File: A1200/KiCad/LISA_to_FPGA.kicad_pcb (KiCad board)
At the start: 2 copper layers, 64 x 37 mm, 18 parts, among them J1 Conn_01x04, J2 Conn_01x40, U1 LM1117-3.3, U2 74LVC16244ADGG, U3 74LVC16244ADGG, U4 LISA

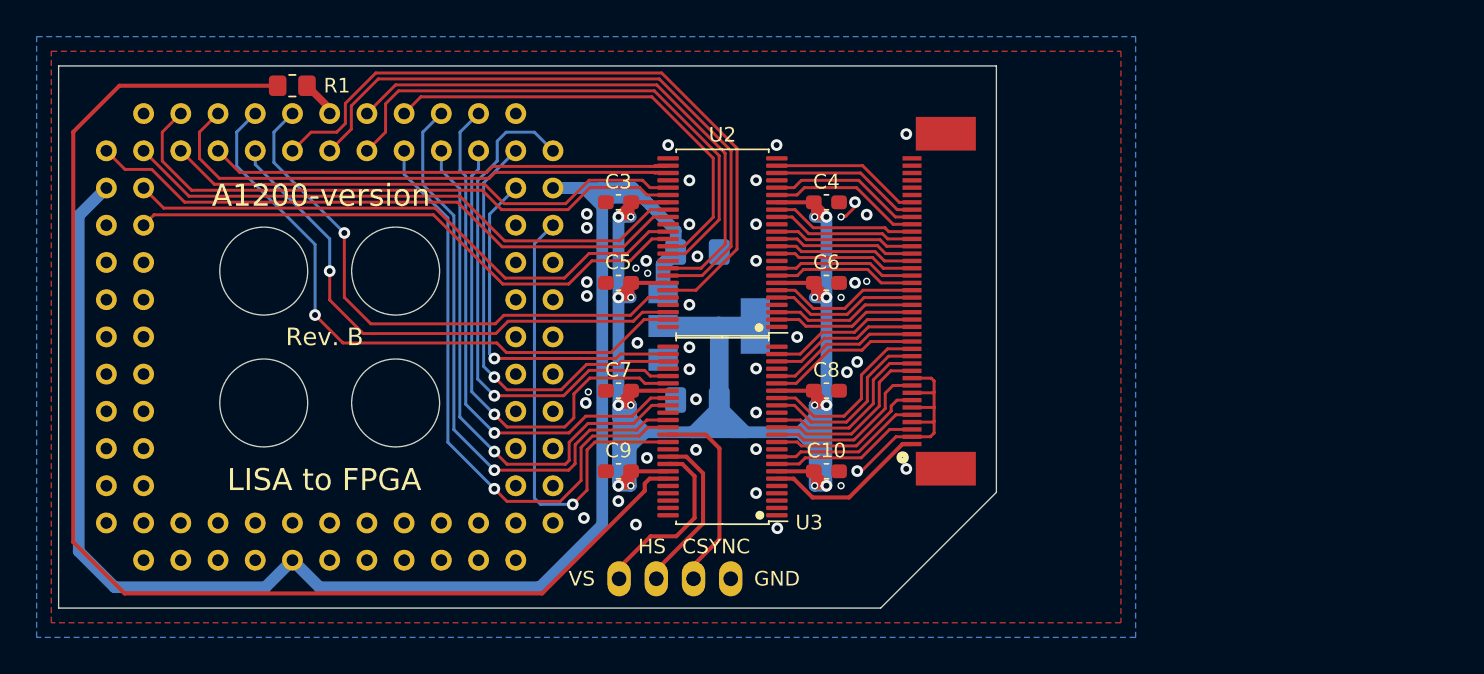
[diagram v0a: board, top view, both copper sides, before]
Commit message: Add a RP2354B to the design
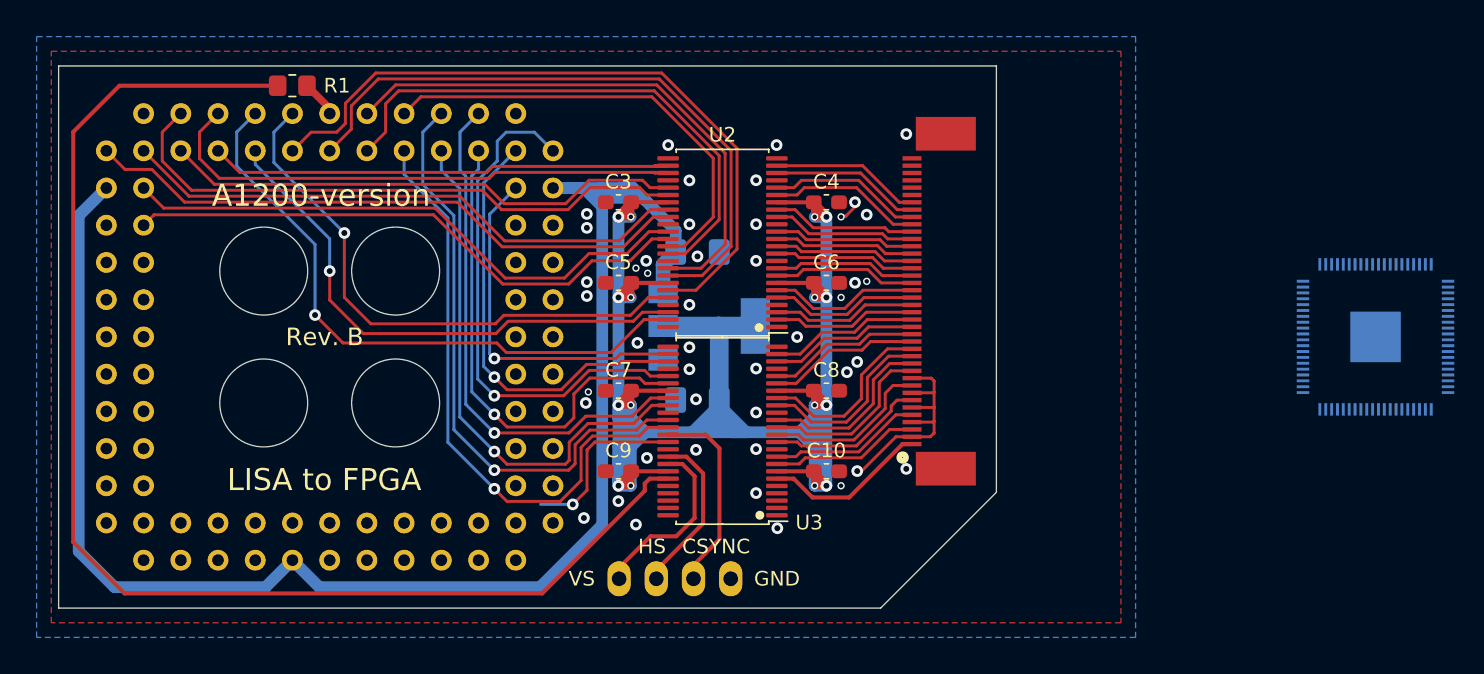
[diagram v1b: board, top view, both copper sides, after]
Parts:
- added U5: SC2212, LISA_to_FPGA:QFN40P1000X1000X90-81N-D, B.Cu at (238.1, 90.4)
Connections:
- net Net-(U4-Pad23) renamed C14O
- U4 pad 12: Net-(U4-Pad12) -> RGA8
- U4 pad 13: Net-(U4-Pad13) -> RGA7
- U4 pad 14: Net-(U4-Pad14) -> RGA6
- U4 pad 15: Net-(U4-Pad15) -> RGA5
- U4 pad 16: Net-(U4-Pad16) -> RGA4
- U4 pad 17: Net-(U4-Pad17) -> RGA3
- U4 pad 18: Net-(U4-Pad18) -> RGA2
- U4 pad 19: Net-(U4-Pad19) -> RGA1
- U4 pad 28: PIXELSW -> Net-(U4-Pad28)
- U4 pad 59: Net-(U4-Pad59) -> D31
- U4 pad 60: Net-(U4-Pad60) -> D30
- U4 pad 61: Net-(U4-Pad61) -> D29
- U4 pad 62: Net-(U4-Pad62) -> D28
- U4 pad 63: Net-(U4-Pad63) -> D27
- U4 pad 64: Net-(U4-Pad64) -> D26
- U4 pad 65: Net-(U4-Pad65) -> D25
- U4 pad 66: Net-(U4-Pad66) -> D24
- U4 pad 67: Net-(U4-Pad67) -> D23
- U4 pad 68: Net-(U4-Pad68) -> D22
- U4 pad 69: Net-(U4-Pad69) -> D21
- U4 pad 70: Net-(U4-Pad70) -> D20
- U4 pad 71: Net-(U4-Pad71) -> D19
- U4 pad 72: Net-(U4-Pad72) -> D18
- U4 pad 73: Net-(U4-Pad73) -> D17
- U4 pad 74: Net-(U4-Pad74) -> D16
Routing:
- net PIXELSW: track 31.8 -> 12.1 mm

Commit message: Change single resistors to 0603, add 330 OHm resistor packs, change U2,U3 to 74LVC162244ADGG with built-in 30 ohm termination resistors, fix to handsolder footprint for RP2354B, pin assignment and more routing
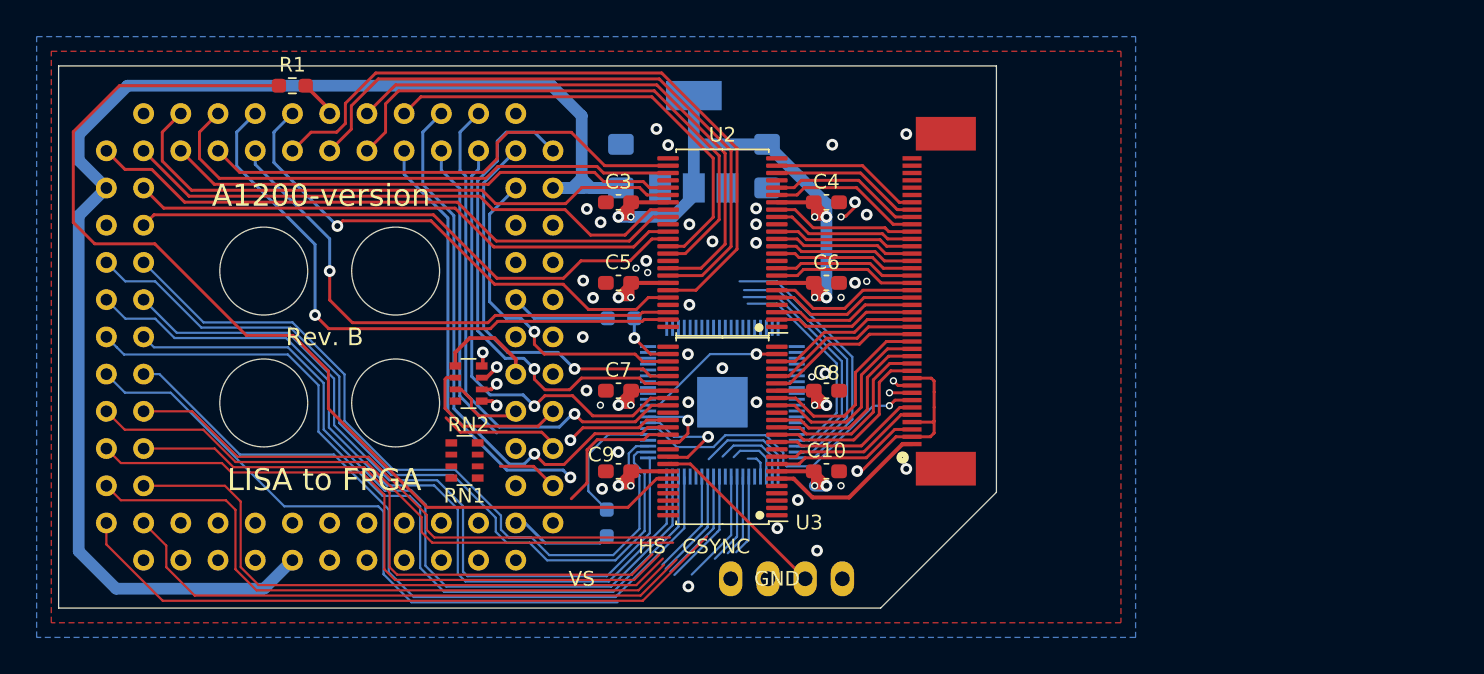
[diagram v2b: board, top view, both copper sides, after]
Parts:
- added R2: 330, Resistor_SMD:R_0603_1608Metric_Pad0.98x0.95mm_HandSolder, B.Cu at (185.7, 103.1)
- added R3: 100, Resistor_SMD:R_0603_1608Metric_Pad0.98x0.95mm_HandSolder, B.Cu at (186.6, 89.2)
- added RN1: R_Pack04, Resistor_SMD:R_Array_Convex_4x0603, F.Cu at (176.0, 98.9)
- added RN2: R_Pack04, Resistor_SMD:R_Array_Convex_4x0603, F.Cu at (176.2, 93.6)
- R1: value 33Ω -> 68; footprint Resistor_SMD:R_0805_2012Metric_Pad1.20x1.40mm_HandSolder -> Resistor_SMD:R_0603_1608Metric_Pad0.98x0.95mm_HandSolder
- U2, U3: value 74LVC16244ADGG -> 74LVC162244ADGG
- moved U5 44.8 mm to (193.6, 94.9), turned to 90 degrees
- moved C2 16.7 mm to (196.6, 78.8), turned to 90 degrees
- moved U1 12.6 mm to (191.6, 77.1), turned to 90 degrees
- moved C1 7.85 mm to (186.6, 78.8), turned to 270 degrees
- moved J1 7.62 mm to (201.8, 106.9)
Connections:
- net HSYNC_3V3 renamed LINK_D0_BUF
- net Net-(U5-Pad66) renamed USB_DM
- net Net-(U5-Pad67) renamed USB_DP
- J2 pad 3: VSYNC_3V3 -> CSYNC_3V3
- J2 pad 6: GND -> LINK_D1_BUF
- J2 pad 7: PIXELSW_3V3 -> LINK_RET
- J2 pad 8: GND -> TX
- J2 pad 9: CSYNC_3V3 -> RX
- U3 pad 11: PIXELSW_3V3 -> LINK_D1_BUF
- U3 pad 12: CSYNC_3V3 -> B7_3V3
- U3 pad 13: B7_3V3 -> B6_3V3
- U3 pad 14: B6_3V3 -> B5_3V3
- U3 pad 16: B5_3V3 -> B4_3V3
- U3 pad 17: B4_3V3 -> B3_3V3
- U3 pad 19: B3_3V3 -> B2_3V3
- U3 pad 20: B2_3V3 -> B1_3V3
- U3 pad 22: B1_3V3 -> B0_3V3
- U3 pad 23: B0_3V3 -> C14O_3V3
- U3 pad 26: B0 -> Net-(R3-Pad1)
- U3 pad 27: B1 -> B0
- U3 pad 29: B2 -> B1
- U3 pad 30: B3 -> B2
- U3 pad 32: B4 -> B3
- U3 pad 33: B5 -> B4
- U3 pad 35: B6 -> B5
- U3 pad 36: B7 -> B6
- U3 pad 37: CSYNC -> B7
- U3 pad 38: PIXELSW -> LINK_D1
- U3 pad 40: HSYNC -> LINK_D0
- U3 pad 41: VSYNC -> CSYNC
- U3 pad 8: VSYNC_3V3 -> CSYNC_3V3
- U4 pad 10: Net-(U4-Pad10) -> CCK
- U4 pad 12: RGA8 -> /RGA88
- U4 pad 13: RGA7 -> /RGA77
- U4 pad 14: RGA6 -> /RGA66
- U4 pad 15: RGA5 -> /RGA55
- U4 pad 16: RGA4 -> /RGA44
- U4 pad 17: RGA3 -> /RGA33
- U4 pad 18: RGA2 -> /RGA22
- U4 pad 19: RGA1 -> /RGA11
- U5 pad 15: Net-(U5-Pad15) -> 3V3
- U5 pad 24: Net-(U5-Pad24) -> 3V3
- U5 pad 25: CCK -> Net-(R2-Pad1)
- U5 pad 29: Net-(U5-Pad29) -> 3V3
- U5 pad 30: XIN -> C14O_3V3
- U5 pad 36: Net-(U5-Pad36) -> TX
- U5 pad 37: Net-(U5-Pad37) -> RX
- U5 pad 41: Net-(U5-Pad41) -> 3V3
- U5 pad 5: Net-(U5-Pad5) -> 3V3
- U5 pad 50: Net-(U5-Pad50) -> 3V3
- U5 pad 60: Net-(U5-Pad60) -> 3V3
- U5 pad 76: Net-(U5-Pad76) -> 3V3
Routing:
- net 3V3: track 180.2 -> 90.8 mm, vias 16 -> 17
- net D26: track 0.00 -> 55.8 mm
- net D28: track 0.00 -> 55.5 mm
- net D30: track 0.00 -> 54.9 mm
- net D29: track 0.00 -> 53.3 mm
- net D20: track 0.00 -> 53.1 mm
- net D27: track 0.00 -> 52.5 mm
- net D31: track 0.00 -> 52.2 mm
- net D16: track 0.00 -> 51.4 mm
- net D25: track 0.00 -> 51.2 mm
- net D22: track 0.00 -> 50.5 mm
- net D18: track 0.00 -> 50.4 mm
- net D21: track 0.00 -> 49.6 mm
- net D19: track 0.00 -> 49.4 mm
- net D23: track 0.00 -> 47.2 mm
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
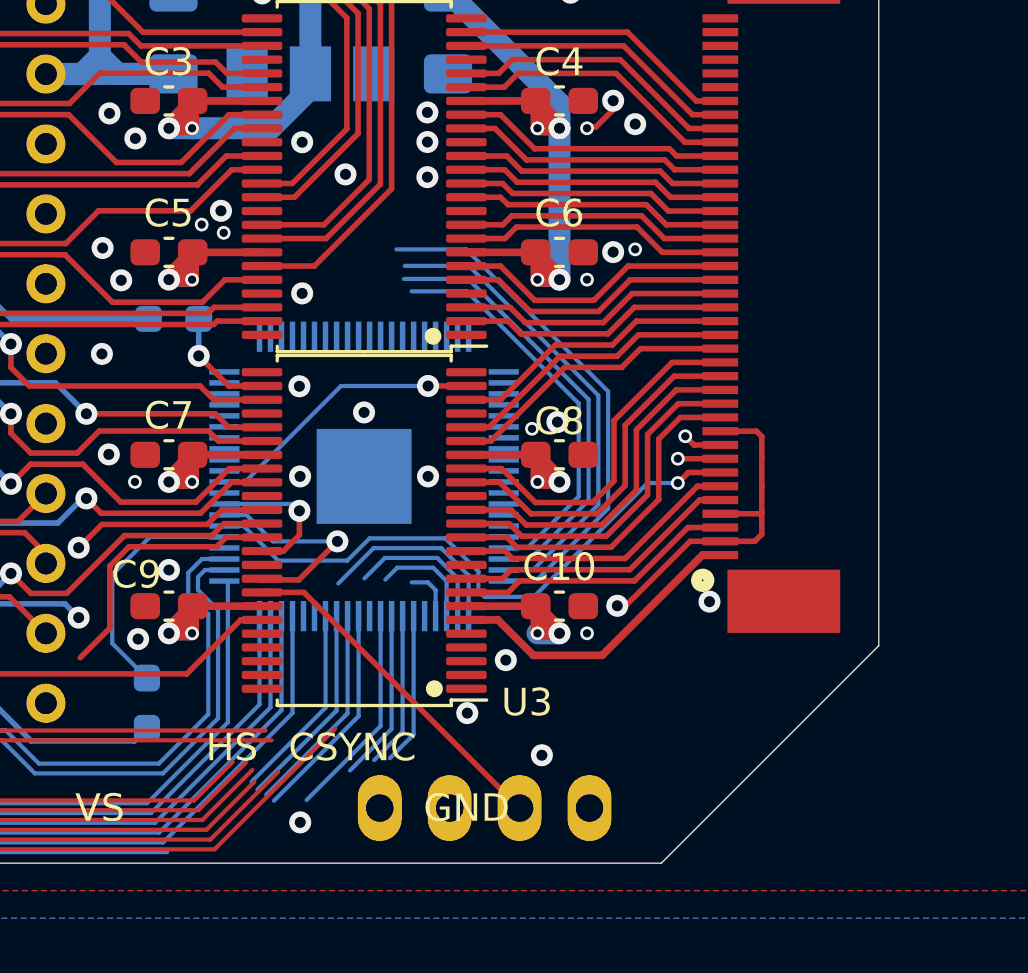
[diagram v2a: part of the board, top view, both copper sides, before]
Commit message: Add power circuit for 1.1V
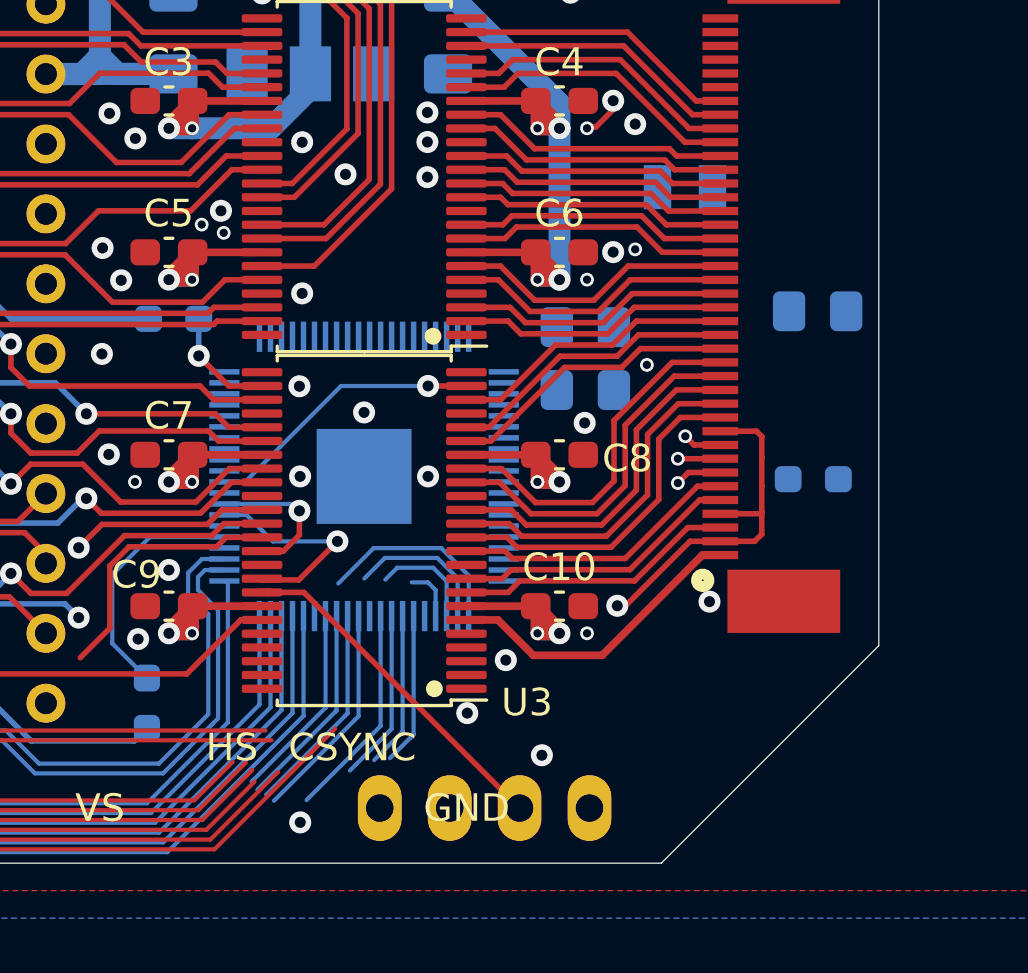
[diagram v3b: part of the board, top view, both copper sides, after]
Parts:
- added C11: 4.7uF, Capacitor_SMD:C_0805_2012Metric_Pad1.18x1.45mm_HandSolder, B.Cu at (201.6, 89.5)
- added C12: 4.7uF, Capacitor_SMD:C_0805_2012Metric_Pad1.18x1.45mm_HandSolder, B.Cu at (210.0, 88.9)
- added C13: 4.7uF, Capacitor_SMD:C_0805_2012Metric_Pad1.18x1.45mm_HandSolder, B.Cu at (201.6, 91.7)
- added L1: 3.3uH, LISA_to_FPGA:AOTAB201610S3R3101T, B.Cu at (205.2, 84.4)
- added R4: 33, Resistor_SMD:R_0603_1608Metric_Pad0.98x0.95mm_HandSolder, B.Cu at (209.9, 95.0)
- U5: value SC2212 -> RP2354B
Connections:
- net Net-(U5-Pad33) renamed /SWCLK
- net Net-(U5-Pad34) renamed /SWDIO
- net Net-(U5-Pad35) renamed /RUN
- U5 pad 10: Net-(U5-Pad10) -> 1V1
- U5 pad 32: Net-(U5-Pad32) -> 1V1
- U5 pad 51: Net-(U5-Pad51) -> 1V1
- U5 pad 59: Net-(U5-Pad59) -> 3V3
- U5 pad 61: Net-(U5-Pad61) -> /VREG_AVDD
- U5 pad 62: Net-(U5-Pad62) -> GND
- U5 pad 63: Net-(U5-Pad63) -> /VREG_LX
- U5 pad 64: Net-(U5-Pad64) -> 3V3
- U5 pad 65: Net-(U5-Pad65) -> 1V1
- U5 pad 68: Net-(U5-Pad68) -> 3V3
- U5 pad 69: Net-(U5-Pad69) -> 3V3
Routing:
- net LINK_RET: track 22.0 -> 1.70 mm
- net RGA4: track 20.1 -> 1.15 mm
- net RGA3: track 18.6 -> 1.18 mm
- net RGA2: track 17.5 -> 1.34 mm
- net RGA1: track 15.6 -> 0.96 mm
- net D24: track 43.8 -> 54.5 mm
- net 3V3: track 90.8 -> 91.6 mm

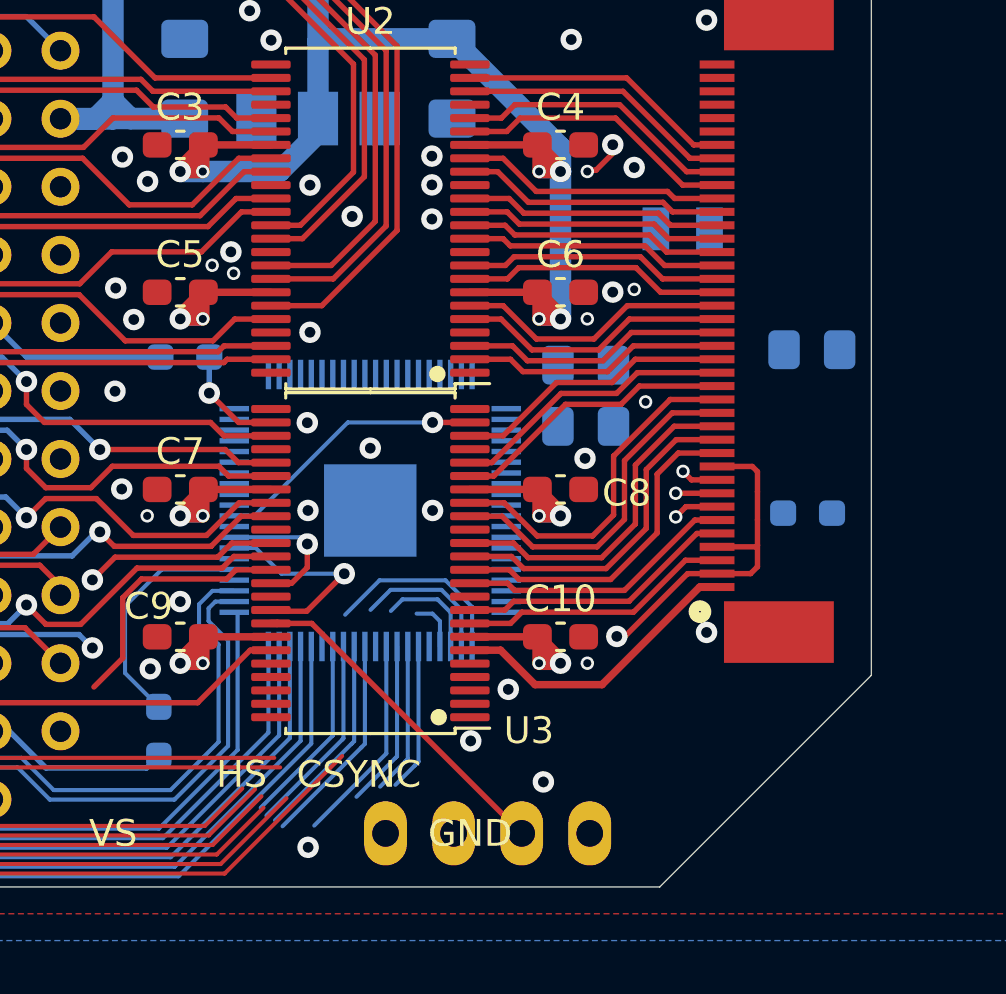
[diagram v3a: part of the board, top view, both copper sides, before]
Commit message: Add routing of 1.1V
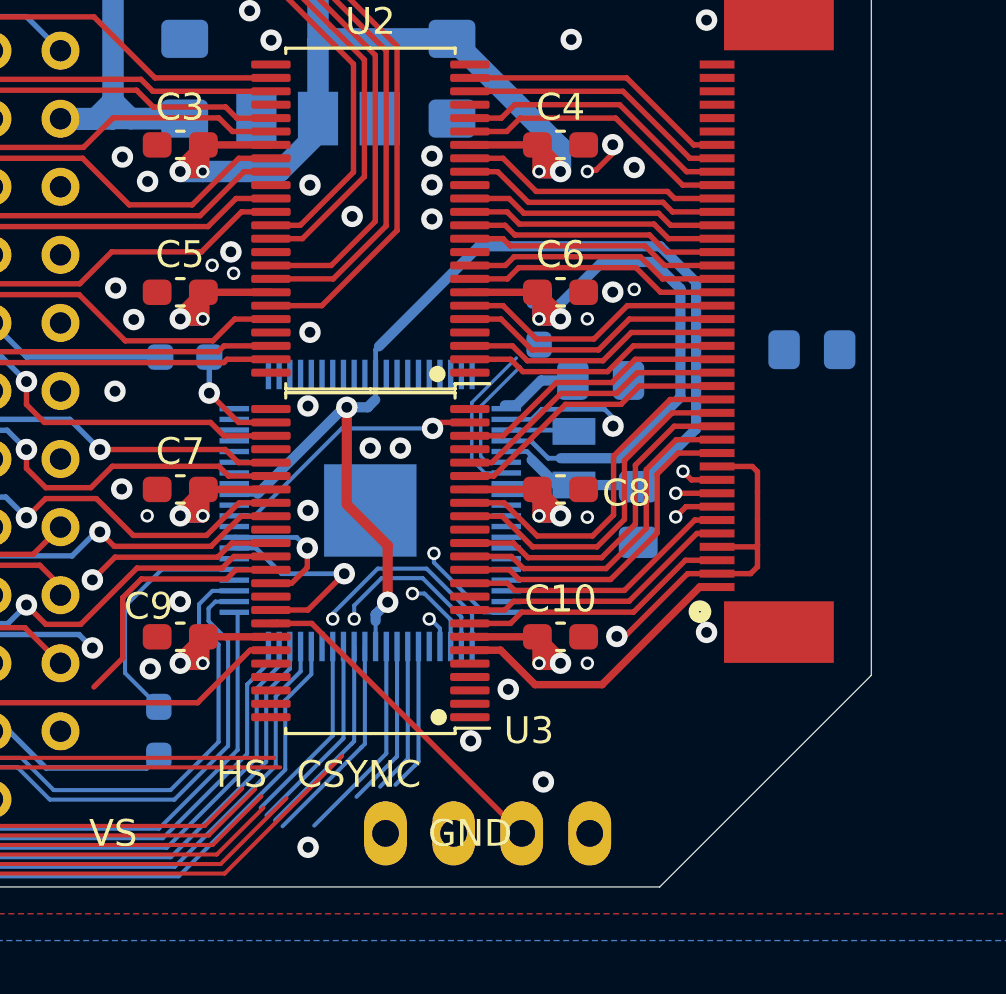
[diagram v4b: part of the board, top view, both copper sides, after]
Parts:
- moved R4 12.3 mm to (199.9, 87.8), turned to 270 degrees
- moved L1 9.47 mm to (201.2, 92.9), turned to 90 degrees
- moved C13 3.83 mm to (203.6, 95.0), turned to 270 degrees
- moved C11 0.80 mm to (202.2, 90.0)
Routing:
- net 1V1: track 0.00 -> 48.1 mm, vias 0 -> 2
- net 3V3: track 91.6 -> 114.2 mm
- net USB_DP: track 0.00 -> 5.98 mm
- net USB_DM: track 0.00 -> 4.99 mm
- net GND: track 14.9 -> 19.5 mm
- net RGA4: track 1.15 -> 4.96 mm, vias 1 -> 2
- net /VREG_AVDD: track 0.00 -> 2.92 mm
- net /VREG_LX: track 0.00 -> 2.55 mm
- net RGA6: track 5.38 -> 6.63 mm, vias 0 -> 1
- net RGA7: track 3.88 -> 2.83 mm, vias 0 -> 1
- net RGA5: track 7.16 -> 8.01 mm, vias 0 -> 1
- net RGA8: track 1.93 -> 1.22 mm, vias 0 -> 1
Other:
- rule trace_min: 0.1524 -> 0.127
